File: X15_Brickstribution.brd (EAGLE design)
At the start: 87 parts, among them Q1 310mA/60V/1.6Ω, U5 IC_L4970A, U6 DIODE_STPS1545CT, U7 IC_L4970A, U8 DIODE_STPS1545CT

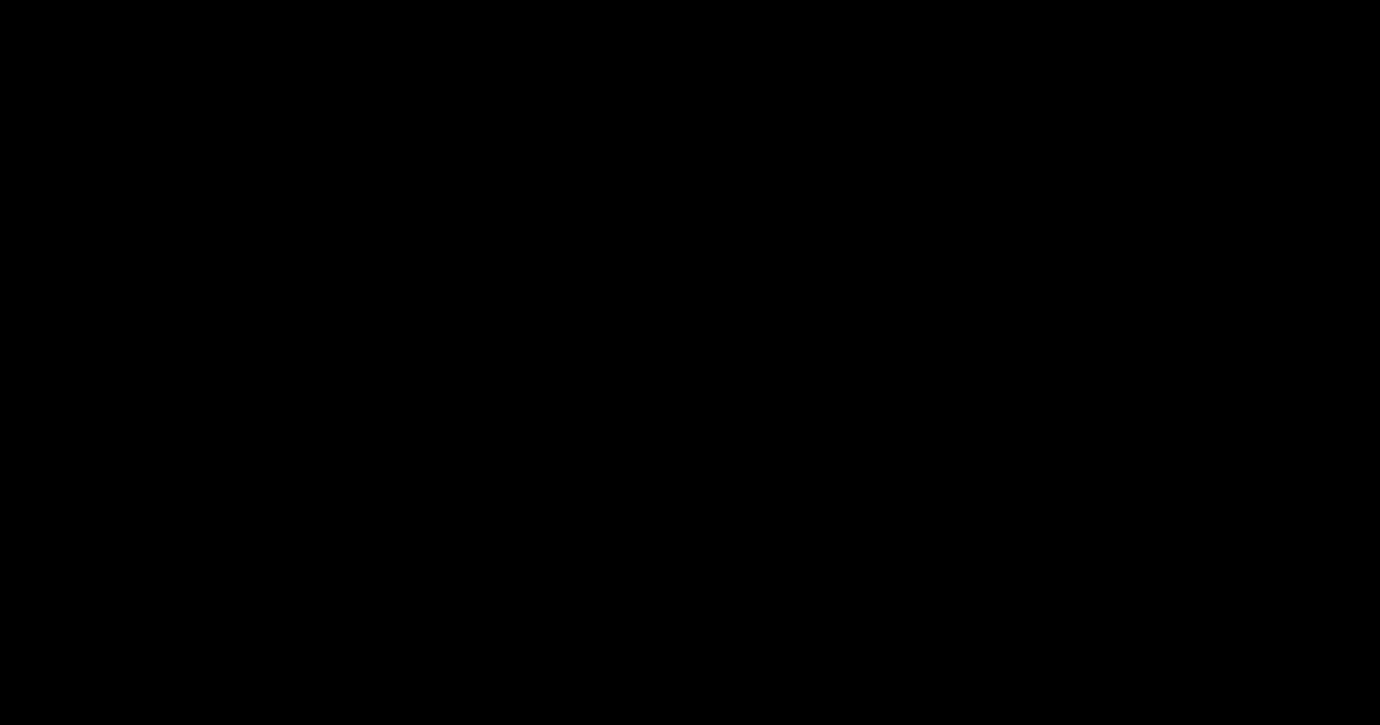
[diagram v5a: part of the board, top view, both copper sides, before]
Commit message: board dimensions
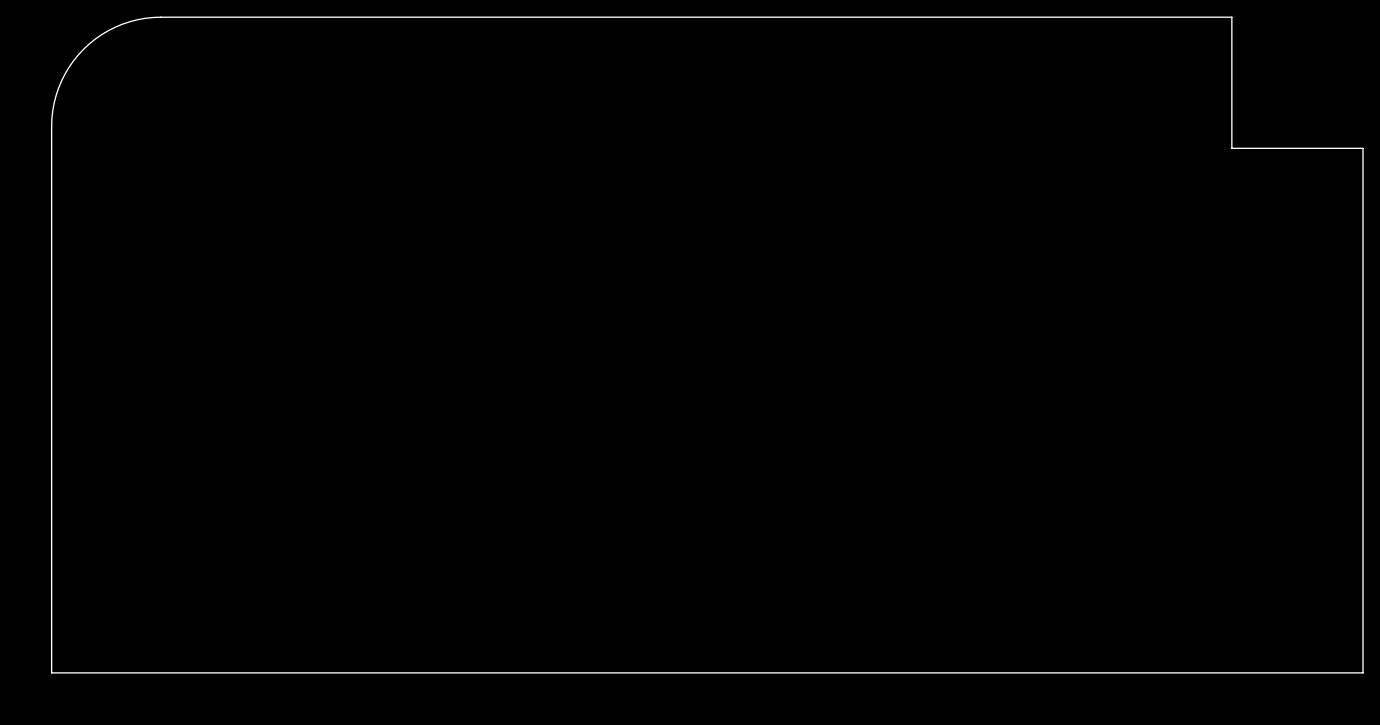
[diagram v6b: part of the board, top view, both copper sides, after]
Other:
- board outline added: 152.4 x 76.2 mm
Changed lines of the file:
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@@
 <setting verticaltext="up"/>
 </settings>
-<grid distance="50" unitdist="mil" unit="mil" style="lines" multiple="1" display="no" altdistance="5" altunitdist="mil" altunit="mil"/>
+<grid distance="1" unitdist="mil" unit="mil" style="lines" multiple="1" display="no" altdistance="5" altunitdist="mil" altunit="mil"/>
 <layers>
 <layer number="1" name="Top" color="4" fill="1" visible="yes" active="yes"/>
@@
 <layer number="154" name="FabDoc2" color="7" fill="1" visible="yes" active="yes"/>
 <layer number="155" name="FabDoc3" color="7" fill="1" visible="yes" active="yes"/>
+<layer number="166" name="AntennaArea" color="7" fill="1" visible="yes" active="yes"/>
+<layer number="168" name="4mmHeightArea" color="7" fill="1" visible="yes" active="yes"/>
 <layer number="191" name="mNets" color="7" fill="1" visible="yes" active="yes"/>
 <layer number="192" name="mBusses" color="7" fill="1" visible="yes" active="yes"/>
@@
 <board>
 <plain>
+<wire x1="0.1016" y1="0" x2="152.5016" y2="0" width="0" layer="20"/>
+<wire x1="152.5016" y1="0" x2="152.5016" y2="60.96" width="0" layer="20"/>
+<wire x1="0.1016" y1="63.5" x2="0.1016" y2="0" width="0" layer="20"/>
+<wire x1="137.2616" y1="76.2" x2="137.2616" y2="60.96" width="0" layer="20"/>
+<wire x1="137.2616" y1="60.96" x2="152.5016" y2="60.96" width="0" layer="20"/>
+<wire x1="12.8016" y1="76.2" x2="137.2616" y2="76.2" width="0" layer="20"/>
+<wire x1="12.8016" y1="76.2" x2="0.1016" y2="63.5" width="0" layer="20" curve="90"/>
 </plain>
 <attributes>

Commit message: 48V Components Added to PCB
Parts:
- removed U$1: IRF1018E_S_SLPBF, X15_Brickstribution:IRF1018E_S_SLPBF
- added REV_TRANS: TRANS_IRF1018E_S_SLPBF, X15_Brickstribution:IRF1018E_S_SLPBF
- BACKPLANE_POWER, U$7: device X15_Brickstribution:MPPT-10-01-01-L-RA-SD(PLACEHOLDER) -> X15_Brickstribution:MPPT-10-01-01-L-RA-SD
- moved U$2 937.2 mm to (34.9, 67.6), flipped to the bottom, turned to 180 degrees
- moved +7.4V_SERVO_TEST 656.0 mm to (100.7, -29.7)
- moved 7.4V_GND 656.0 mm to (100.7, -22.1)
- moved C22 656.0 mm to (105.7, -183.4)
- moved C23 656.0 mm to (109.6, -183.4)
- moved C24 656.0 mm to (113.4, -183.4)
- moved C25 656.0 mm to (117.2, -183.4)
- moved C26 656.0 mm to (121.0, -183.4)
- moved C27 656.0 mm to (124.8, -183.4)
- moved C28 656.0 mm to (128.6, -183.4)
- moved C29 656.0 mm to (178.1, -102.1)
- moved C30 656.0 mm to (132.4, -183.4)
- moved C31 656.0 mm to (136.2, -183.4)
- moved C32 656.0 mm to (140.0, -183.4)
- moved C33 656.0 mm to (143.8, -183.4)
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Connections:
- removed net N$1: D1.C, R1.1, U$1.P$1
- removed net N$2: U$2.PIN4
- removed net N$3: U$2.PIN7
- new net REV_GATE: D1.C, R1.1, REV_TRANS.P$1
- net +12V: now also U$2.PIN7
- net +12V_CONV: now also BACKPLANE_POWER.1@1, BACKPLANE_POWER.1@2, BACKPLANE_POWER.1@3, BACKPLANE_POWER.1@4, BACKPLANE_POWER.1@5, BACKPLANE_POWER.1@6, BACKPLANE_POWER.2@1, BACKPLANE_POWER.2@2, BACKPLANE_POWER.2@3, BACKPLANE_POWER.2@4, BACKPLANE_POWER.2@5, BACKPLANE_POWER.2@6, BACKPLANE_POWER.3@1, BACKPLANE_POWER.3@2, BACKPLANE_POWER.3@3, BACKPLANE_POWER.3@4, BACKPLANE_POWER.3@5, BACKPLANE_POWER.3@6, BACKPLANE_POWER.4@1, BACKPLANE_POWER.4@2, BACKPLANE_POWER.4@3, BACKPLANE_POWER.4@4, BACKPLANE_POWER.4@5, BACKPLANE_POWER.4@6, BACKPLANE_POWER.5@1, BACKPLANE_POWER.5@2, BACKPLANE_POWER.5@3, BACKPLANE_POWER.5@4, BACKPLANE_POWER.5@5, BACKPLANE_POWER.5@6; no longer BACKPLANE_POWER.2, BACKPLANE_POWER.3, BACKPLANE_POWER.4, BACKPLANE_POWER.5, BACKPLANE_POWER.6
- net +7.4V_SERVO: now also U$7.1@1, U$7.1@2, U$7.1@3, U$7.1@4, U$7.1@5, U$7.1@6, U$7.2@1, U$7.2@2, U$7.2@3, U$7.2@4, U$7.2@5, U$7.2@6, U$7.3@1, U$7.3@2, U$7.3@3, U$7.3@4, U$7.3@5, U$7.3@6, U$7.4@1, U$7.4@2, U$7.4@3, U$7.4@4, U$7.4@5, U$7.4@6, U$7.5@1, U$7.5@2, U$7.5@3, U$7.5@4, U$7.5@5, U$7.5@6; no longer U$7.2, U$7.3, U$7.4, U$7.5, U$7.6
- net 12V_GND: now also BACKPLANE_POWER.10@1, BACKPLANE_POWER.10@2, BACKPLANE_POWER.10@3, BACKPLANE_POWER.10@4, BACKPLANE_POWER.10@5, BACKPLANE_POWER.10@6, BACKPLANE_POWER.6@1, BACKPLANE_POWER.6@2, BACKPLANE_POWER.6@3, BACKPLANE_POWER.6@4, BACKPLANE_POWER.6@5, BACKPLANE_POWER.6@6, BACKPLANE_POWER.7@1, BACKPLANE_POWER.7@2, BACKPLANE_POWER.7@3, BACKPLANE_POWER.7@4, BACKPLANE_POWER.7@5, BACKPLANE_POWER.7@6, BACKPLANE_POWER.8@1, BACKPLANE_POWER.8@2, BACKPLANE_POWER.8@3, BACKPLANE_POWER.8@4, BACKPLANE_POWER.8@5, BACKPLANE_POWER.8@6, BACKPLANE_POWER.9@1, BACKPLANE_POWER.9@2, BACKPLANE_POWER.9@3, BACKPLANE_POWER.9@4, BACKPLANE_POWER.9@5, BACKPLANE_POWER.9@6, U$2.PIN4, U$7.10@1, U$7.10@2, U$7.10@3, U$7.10@4, U$7.10@5, U$7.10@6, U$7.6@1, U$7.6@2, U$7.6@3, U$7.6@4, U$7.6@5, U$7.6@6, U$7.7@1, U$7.7@2, U$7.7@3, U$7.7@4, U$7.7@5, U$7.7@6, U$7.8@1, U$7.8@2, U$7.8@3, U$7.8@4, U$7.8@5, U$7.8@6, U$7.9@1, U$7.9@2, U$7.9@3, U$7.9@4, U$7.9@5, U$7.9@6; no longer BACKPLANE_POWER.10, BACKPLANE_POWER.11, BACKPLANE_POWER.7, BACKPLANE_POWER.8, BACKPLANE_POWER.9, U$7.10, U$7.11, U$7.7, U$7.8, U$7.9
- net 48V_GND: now also REV_TRANS.P$3; no longer U$1.P$3
- net GND_RAW: now also REV_TRANS.P$2; no longer U$1.P$2
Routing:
- net +48V: track 0.00 -> 70.7 mm, vias 0 -> 3
- net 48V_GND: track 0.00 -> 25.0 mm, vias 0 -> 3
- net ON/OFF: track 0.00 -> 20.3 mm
- net N$7: track 0.00 -> 7.53 mm, vias 0 -> 2
- net REV_GATE: track 0.00 -> 7.43 mm
- net N$6: track 0.00 -> 4.78 mm
- net N$4: track 0.00 -> 1.43 mm
- net N$5: track 0.00 -> 1.18 mm
- added copper zone on layer 16, net +48V
- added copper zone on layer 16, net 48V_GND
- added copper zone on layer 16, net GND_RAW

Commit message: Board & Schematic Review Iteration
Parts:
- removed CONV_CONN: TSW-110-07-G-S, X15_Brickstribution:CON10_1X10_TU_TSW
- removed R2, R3, R4, R5: 10k, SparkFun-Resistors:0603
- removed U$7: CONN_MPPT-10-01-01-L-RA-SD, X15_Brickstribution:MPPT-10-01-01-L-RA-SD
- added H1, H2, H3, H4: 6-32-HOLE, X15_Brickstribution:6-32-HOLE
- added J1: IPL1-104-01-X-S-K, X15_Brickstribution:SAMTEC_IPL1-104-01-X-S-K
- added U$1: CONN_DISTRIBUTION_TO_CONVERSION, X15_Brickstribution:TSW-105-05-G-S(D-C)
- R31: value DIODE_RBQ30NS45AFHTLTRANS_R5009FNJ_ROM-M -> DIODE_RBQ30NS45AFHTL; device X15_Brickstribution:TRANS_R5009FNJ_ROM-M -> X15_Brickstribution:TRANS_R5009FNJ_ROM
- moved R28 271.6 mm to (99.7, 74.2)
- moved 12V_GND_TEST 266.3 mm to (138.3, 2.24)
- moved R30 262.8 mm to (97.4, 61.3)
- moved D14 260.9 mm to (63.7, 17.3), turned to 180 degrees
- moved R29 259.2 mm to (97.5, 58.9), turned to 180 degrees
- moved R12 258.9 mm to (63.7, 19.3)
- moved +12V_TEST 258.6 mm to (134.9, 2.24)
- moved C39 247.7 mm to (97.5, 55.5), turned to 180 degrees
- moved C37 246.1 mm to (101.3, 55.9)
- moved BACKPLANE_CONN 240.9 mm to (120.9, 6.71), turned to 180 degrees
- moved U8 240.6 mm to (99.7, 65.2), turned to 90 degrees
- moved R27 240.4 mm to (117.1, 48.2), turned to 90 degrees
- moved U7 240.0 mm to (104.2, 73.1), turned to 270 degrees
- moved C36 239.2 mm to (111.0, 51.7), turned to 90 degrees
- moved C35 238.0 mm to (114.0, 51.7), turned to 90 degrees
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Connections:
- removed net ALERT_1: BACKPLANE_CONN.09, R3.1
- removed net ALERT_2: BACKPLANE_CONN.10, R4.1
- removed net C2_1: BACKPLANE_CONN.12
- removed net C2_2: BACKPLANE_CONN.13
- removed net CLK: BACKPLANE_CONN.11, R5.1
- removed net DATA: BACKPLANE_CONN.08, R2.1
- removed net D_GND: 3.3V_GND.1, 5V_GND.1, 7.4V_GND.1, BACKPLANE_CONN.05, BACKPLANE_CONN.06, CONV_CONN.10, CONV_CONN.9, D10.C, D11.C
- removed net NC: U$2.PIN2, U5.13, U5.4, U5.5, U7.13, U7.4, U7.5
- net +12V: no longer +12V_TEST.1, R9.1
- net +12V_CONV: now also +12V_TEST.1, R9.1, U$1.1, U$1.2; no longer CONV_CONN.1, CONV_CONN.2
- net +3.3V: now also U$1.5, U$1.6; no longer CONV_CONN.7, CONV_CONN.8, R2.2, R3.2, R4.2, R5.2
- net +5V: now also U$1.7, U$1.8; no longer CONV_CONN.5, CONV_CONN.6
- net +7.4V_SERVO: now also J1.01, J1.02, R31.2; no longer R31.1, U$7.1@1, U$7.1@2, U$7.1@3, U$7.1@4, U$7.1@5, U$7.1@6, U$7.2@1, U$7.2@2, U$7.2@3, U$7.2@4, U$7.2@5, U$7.2@6, U$7.3@1, U$7.3@2, U$7.3@3, U$7.3@4, U$7.3@5, U$7.3@6, U$7.4@1, U$7.4@2, U$7.4@3, U$7.4@4, U$7.4@5, U$7.4@6, U$7.5@1, U$7.5@2, U$7.5@3, U$7.5@4, U$7.5@5, U$7.5@6
- net 12V_GND: now also 3.3V_GND.1, 5V_GND.1, 7.4V_GND.1, BACKPLANE_CONN.05, BACKPLANE_CONN.06, D10.C, D11.C, J1.03, J1.04, U$1.10, U$1.3, U$1.4, U$1.9; no longer CONV_CONN.3, CONV_CONN.4, U$7.10@1, U$7.10@2, U$7.10@3, U$7.10@4, U$7.10@5, U$7.10@6, U$7.6@1, U$7.6@2, U$7.6@3, U$7.6@4, U$7.6@5, U$7.6@6, U$7.7@1, U$7.7@2, U$7.7@3, U$7.7@4, U$7.7@5, U$7.7@6, U$7.8@1, U$7.8@2, U$7.8@3, U$7.8@4, U$7.8@5, U$7.8@6, U$7.9@1, U$7.9@2, U$7.9@3, U$7.9@4, U$7.9@5, U$7.9@6
- net VOUT2: now also R31.1; no longer R31.2
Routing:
- net VOUT1: track 0.00 -> 121.7 mm, vias 0 -> 2
- net VOUT2: track 0.00 -> 112.6 mm, vias 0 -> 1
- net OUT2: track 0.00 -> 62.5 mm
- net OUT1: track 0.00 -> 59.4 mm
- net +3.3V: track 0.00 -> 49.1 mm
- net +48V: track 70.7 -> 23.4 mm, vias 3 -> 2
- net +5V: track 0.00 -> 35.8 mm
- net C_OSC2: track 0.00 -> 26.4 mm
- net V_REF_CAP1: track 0.00 -> 25.7 mm
- net SS1: track 0.00 -> 22.0 mm
- net BOOT2: track 0.00 -> 20.8 mm
- net 48V_GND: track 25.0 -> 45.2 mm, vias 3 -> 4
- net FCOMP1: track 0.00 -> 19.9 mm
- net FCOMP2: track 0.00 -> 15.4 mm
- net BOOT_1: track 0.00 -> 10.8 mm
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- added copper zone on layer 16, net +12V
- added copper zone on layer 16, net +12V_CONV
- added copper zone on layer 16, net +7.4V_SERVO
- added copper zone on layer 1, net 12V_GND
